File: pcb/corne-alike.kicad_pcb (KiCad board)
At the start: 2 copper layers, 45 parts, among them SW1 SW_PUSH, SW10 SW_PUSH, SW11 SW_PUSH, SW12 SW_PUSH, SW13 SW_PUSH, SW14 SW_PUSH, SW15 SW_PUSH, SW16 SW_PUSH, SW17 SW_PUSH, SW18 SW_PUSH, SW19 SW_PUSH, SW2 SW_PUSH, SW20 SW_PUSH, SW21 SW_PUSH, SW3 SW_PUSH, SW4 SW_PUSH, SW5 SW_PUSH, SW6 SW_PUSH, SW7 SW_PUSH, SW8 SW_PUSH, SW9 SW_PUSH, U1 nice_nano

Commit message: Place switches and create pcb shape
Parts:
- U1: value nice_nano -> ProMicro
- moved SW6 235.7 mm to (244.2, 40.8)
- moved SW5 210.3 mm to (226.0, 38.5)
- moved SW12 207.4 mm to (244.2, 58.0)
- moved SW4 185.8 mm to (207.8, 36.0)
- moved SW11 182.4 mm to (226.0, 55.8)
- moved SW18 179.2 mm to (244.2, 75.2)
- moved SW3 160.9 mm to (189.5, 38.5)
- moved SW21 159.0 mm to (259.3, 100.7), turned to 60 degrees
- moved SW10 158.4 mm to (207.8, 53.2)
- moved SW17 154.7 mm to (226.0, 73.0)
- moved SW20 142.2 mm to (238.8, 92.5)
- moved U1 140.9 mm to (264.8, 50.8)
- moved SW2 138.4 mm to (171.2, 50.0)
- moved SW9 134.9 mm to (189.5, 55.8)
- moved SW19 134.0 mm to (220.5, 92.5)
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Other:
- board outline added: 130.3 x 85.3 mm

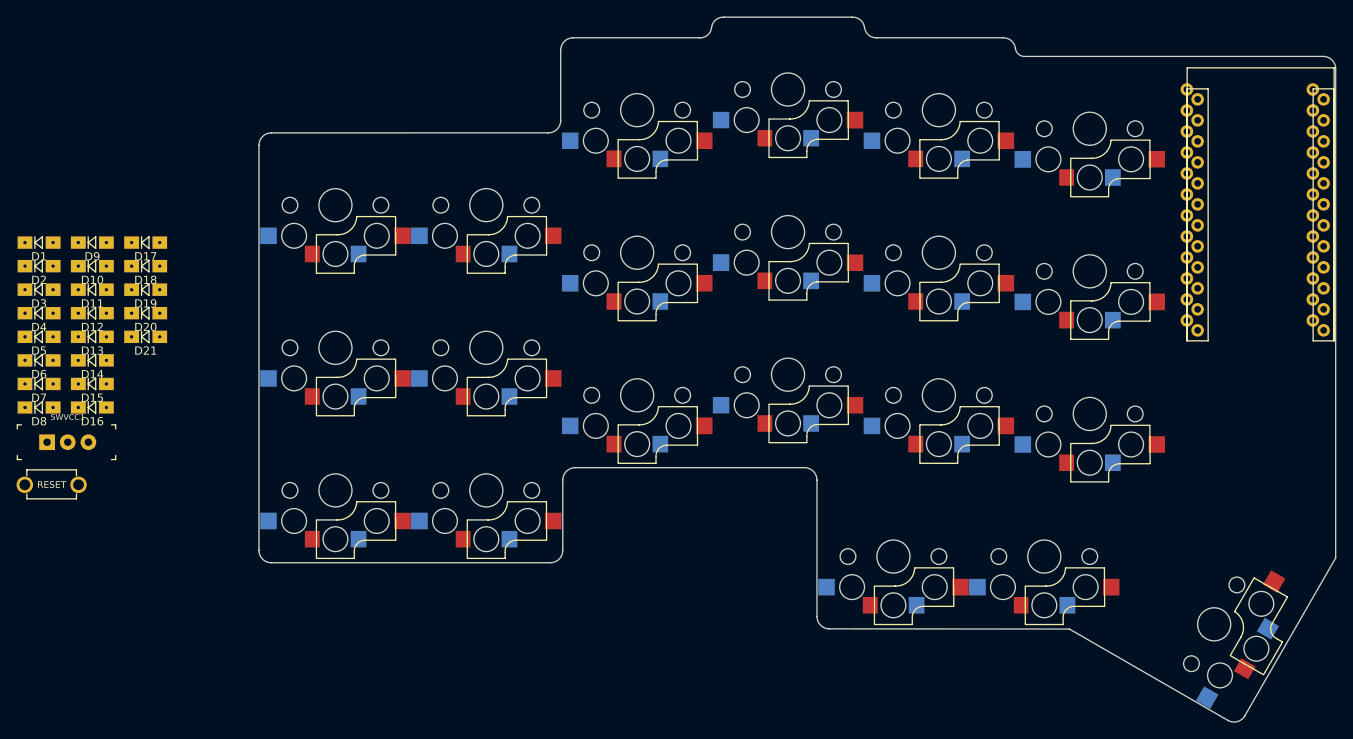
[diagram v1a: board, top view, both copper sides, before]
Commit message: Connect switches and diodes
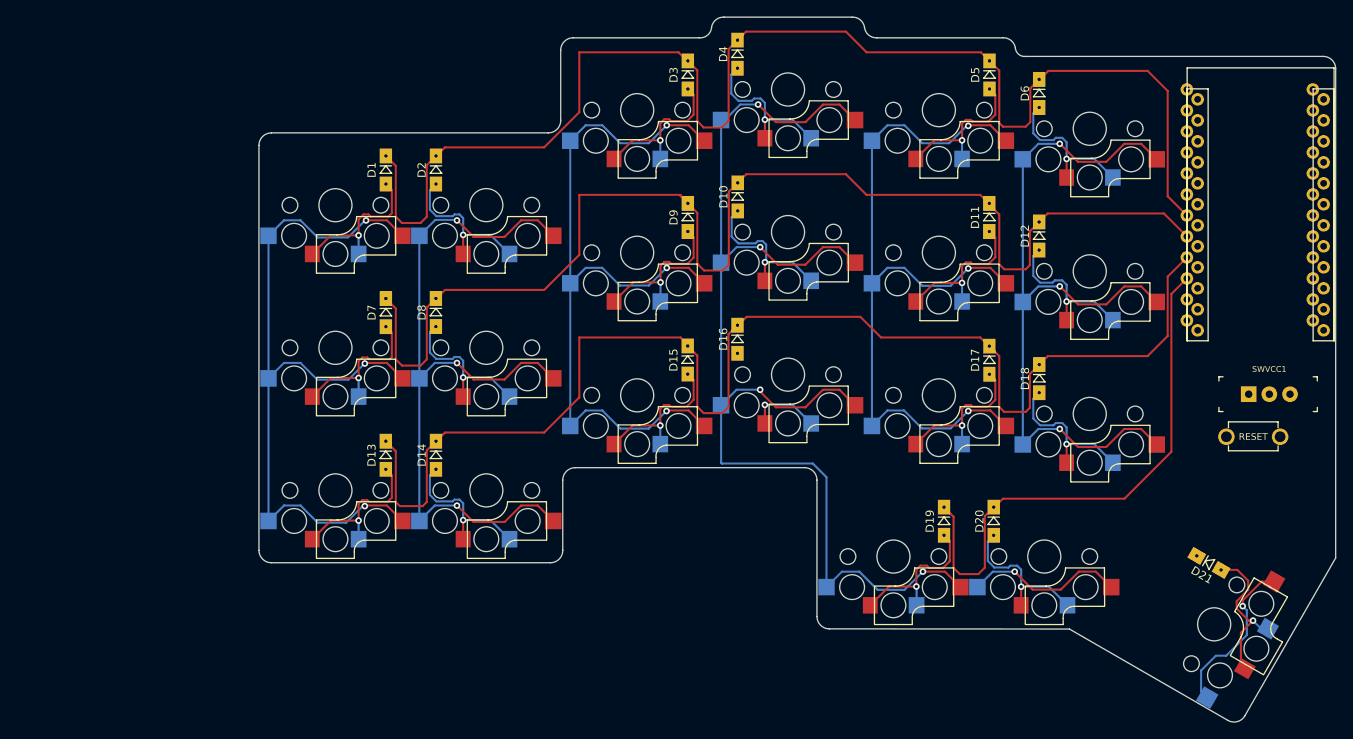
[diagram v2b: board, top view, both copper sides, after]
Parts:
- moved SWVCC1 145.5 mm to (263.5, 72.9)
- moved SWRST1 145.5 mm to (264.0, 78.0)
- moved D21 131.5 mm to (258.7, 93.3), turned to -30 degrees
- moved D6 125.2 mm to (238.1, 36.5), turned to -90 degrees
- moved D5 119.3 mm to (232.1, 34.2), turned to -90 degrees
- moved D12 114.9 mm to (238.1, 53.7), turned to -90 degrees
- moved D18 108.9 mm to (238.1, 71.0), turned to -90 degrees
- moved D11 108.9 mm to (232.1, 51.5), turned to -90 degrees
- moved D20 105.6 mm to (232.6, 88.2), turned to -90 degrees
- moved D17 103.1 mm to (232.1, 68.8), turned to -90 degrees
- moved D19 100.6 mm to (226.6, 88.2), turned to -90 degrees
- moved D4 90.1 mm to (201.6, 31.7), turned to -90 degrees
- moved D3 82.7 mm to (195.6, 34.2), turned to -90 degrees
- moved D10 78.5 mm to (201.7, 49.0), turned to -90 degrees
- moved D16 78.5 mm to (201.6, 66.2), turned to -90 degrees
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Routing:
- net row0: track 0.00 -> 166.3 mm
- net row2: track 0.00 -> 160.3 mm
- net row1: track 0.00 -> 152.6 mm
- net col3: track 0.00 -> 146.5 mm, vias 0 -> 4
- net col5: track 0.00 -> 113.2 mm, vias 0 -> 4
- net col4: track 0.00 -> 112.7 mm, vias 0 -> 4
- net col2: track 0.00 -> 93.4 mm, vias 0 -> 3
- net col0: track 0.00 -> 93.3 mm, vias 0 -> 3
- net col1: track 0.00 -> 92.9 mm, vias 0 -> 3
- net row3: track 0.00 -> 66.0 mm
- net Net-(D10-A): track 0.00 -> 19.2 mm, vias 0 -> 1
- net Net-(D7-A): track 0.00 -> 19.2 mm, vias 0 -> 1
- net Net-(D21-A): track 0.00 -> 19.2 mm, vias 0 -> 1
- net Net-(D1-A): track 0.00 -> 19.1 mm, vias 0 -> 1
- net Net-(D2-A): track 0.00 -> 19.1 mm, vias 0 -> 1
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
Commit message: Connect rows and cols
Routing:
- net col0: track 93.3 -> 240.3 mm, vias 3 -> 13
- net col1: track 92.9 -> 215.7 mm, vias 3 -> 11
- net col2: track 93.4 -> 188.3 mm, vias 3 -> 9
- net col4: track 112.7 -> 202.3 mm, vias 4 -> 6
- net col5: track 113.2 -> 197.1 mm
- net col3: track 146.5 -> 229.7 mm, vias 4 -> 8
- net GND: track 0.00 -> 48.5 mm
- net row3: track 66.0 -> 108.6 mm
- net row2: track 160.3 -> 177.6 mm
- net row0: track 166.3 -> 183.4 mm
- net row1: track 152.6 -> 169.6 mm
- net vcc: track 0.00 -> 14.4 mm
- net reset: track 0.00 -> 14.4 mm
- net Net-(D16-A): track 8.78 -> 19.2 mm

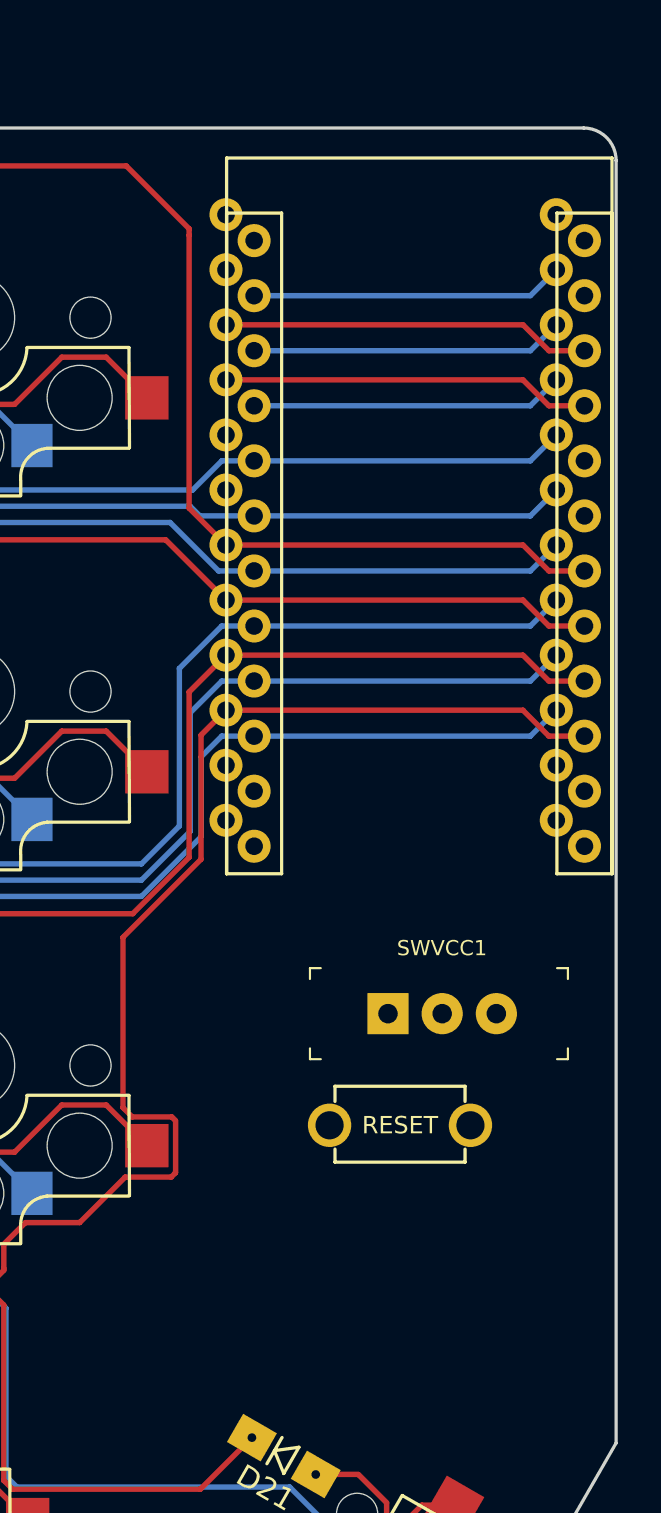
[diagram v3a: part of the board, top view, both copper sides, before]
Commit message: Add bat connector, place reset, on/off and bat to pcb
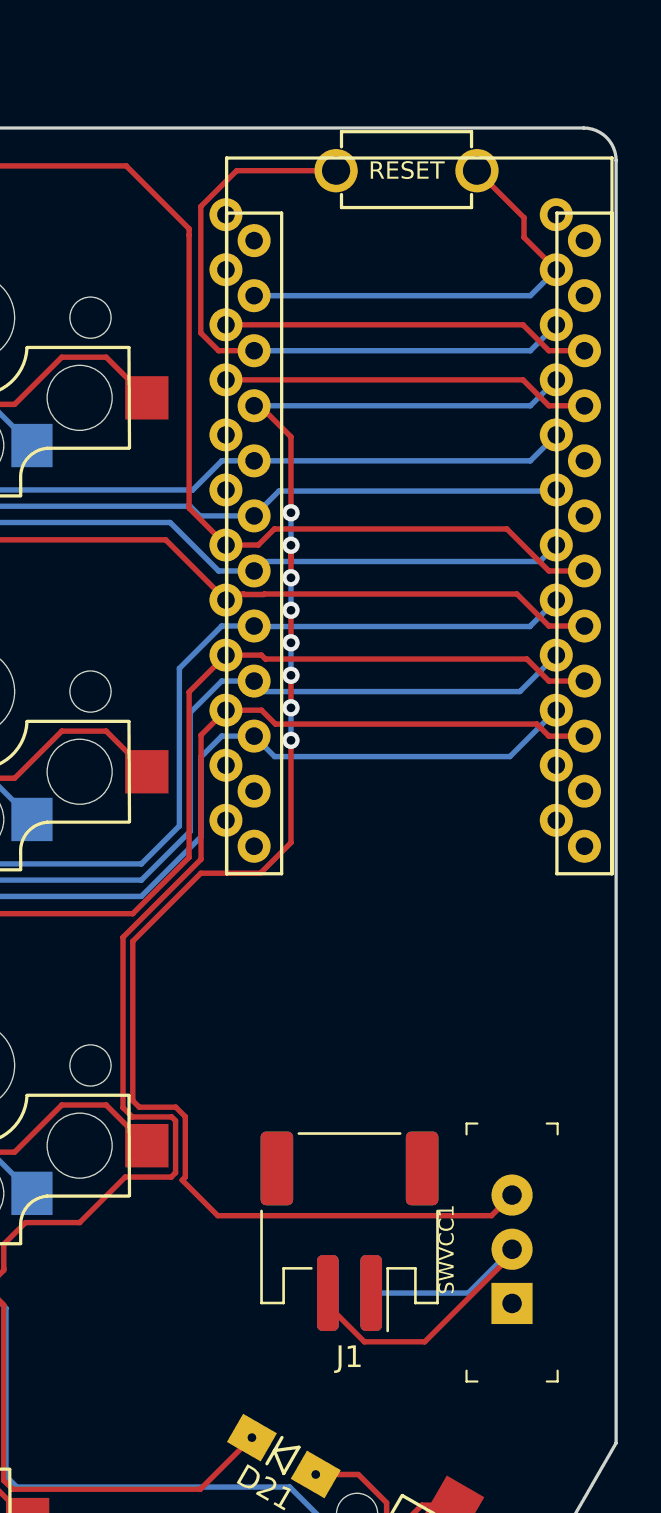
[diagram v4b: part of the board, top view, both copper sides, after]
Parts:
- added J1: Conn_01x02_Socket, corne-alike:JST_PH_S2B-PH-SM4-TB_1x02-1MP_P2.00mm_Horizontal, F.Cu at (261.7, 82.9)
- added J1: Conn_01x02_Socket, corne-alike:JST_PH_S2B-PH-SM4-TB_1x02-1MP_P2.00mm_Horizontal, B.Cu at (261.7, 82.9)
- U1: value ProMicro -> nice_nano
- moved SWRST1 44.0 mm to (264.3, 34.0)
- moved SWVCC1 14.5 mm to (269.2, 86.2), turned to 90 degrees
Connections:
- SWVCC1 pad 2: VCC -> Net-(J1-Pin_2)
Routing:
- net vcc: track 14.4 -> 75.6 mm, vias 0 -> 8
- net Net-(J1-Pin_2): track 0.00 -> 18.8 mm
- net reset: track 14.4 -> 30.1 mm
- net GND: track 48.5 -> 54.6 mm
- net col5: track 197.1 -> 197.9 mm
- net row0: track 183.4 -> 184.0 mm

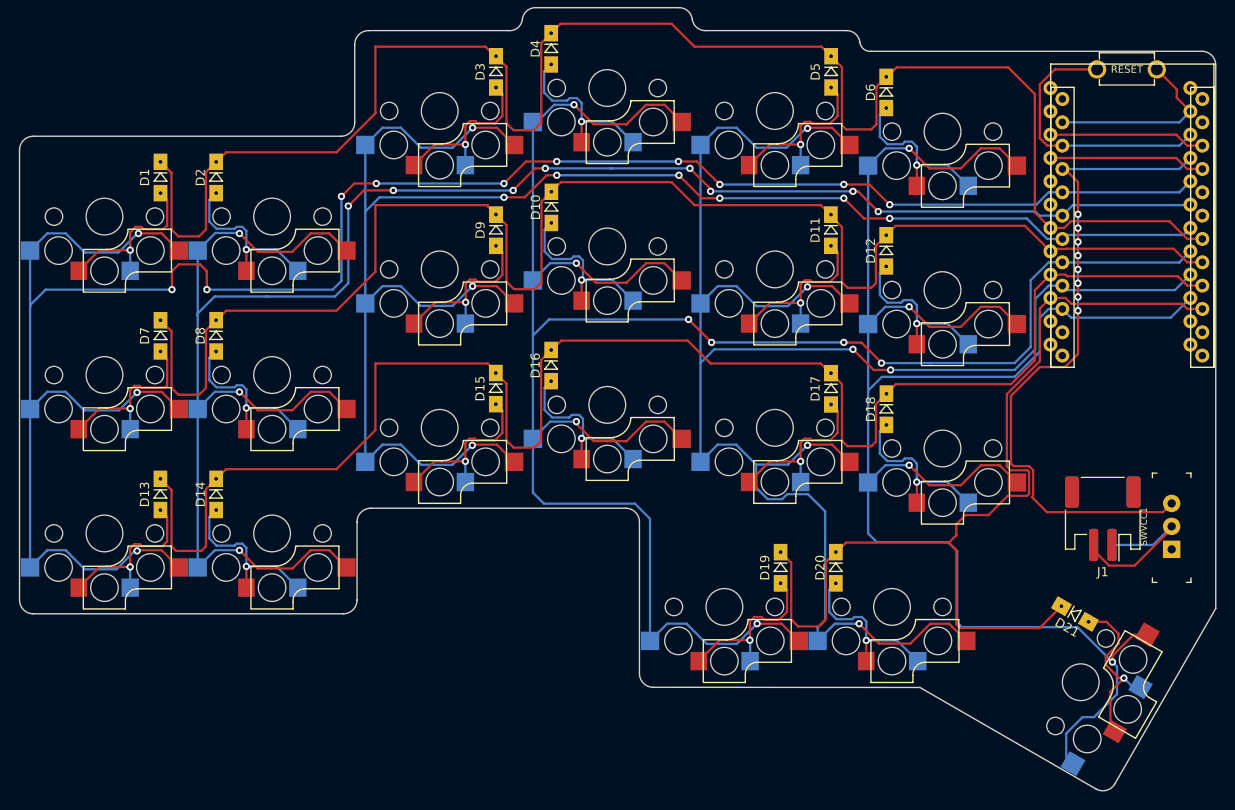
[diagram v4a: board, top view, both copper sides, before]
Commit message: Clean up tracks, drc violations
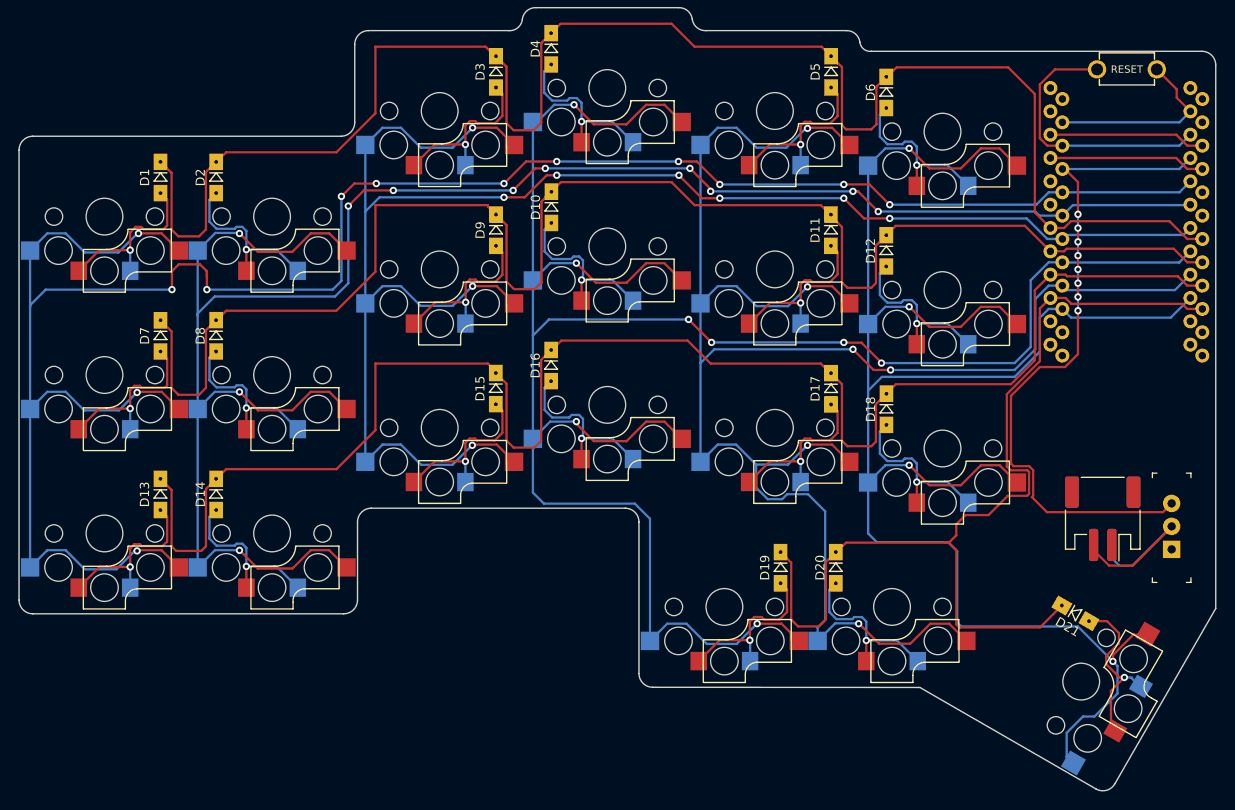
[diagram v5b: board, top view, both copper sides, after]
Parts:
- U1: value nice_nano -> ProMicro
- moved SW21 0.09 mm to (259.4, 100.6)
- moved D21 0.09 mm to (258.7, 93.2)
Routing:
- net Net-(#FLG01-pwr): track 18.8 -> 21.3 mm
- net vcc: track 75.6 -> 74.1 mm
- net col4: track 202.7 -> 201.6 mm
- net col0: track 240.3 -> 239.6 mm
- net Net-(D21-A): track 19.2 -> 18.5 mm
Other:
- outline, holes or cut-outs redrawn

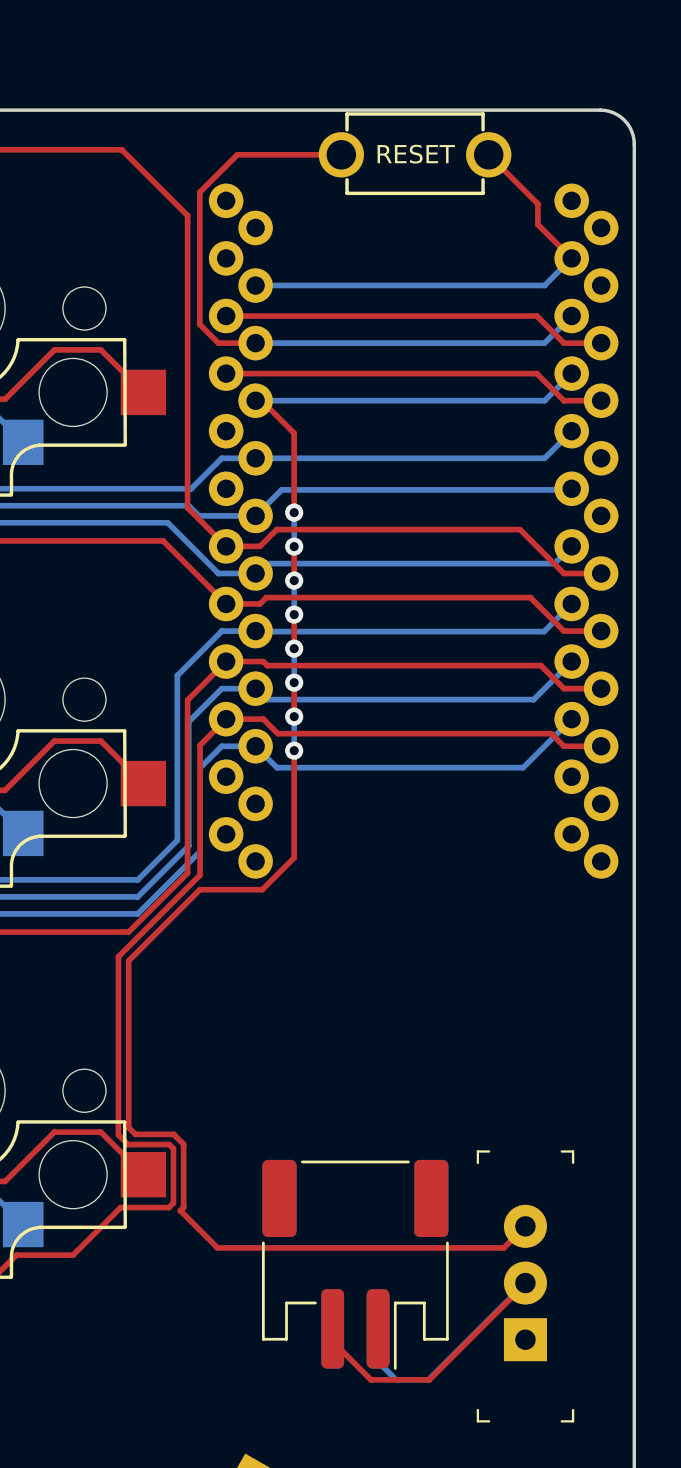
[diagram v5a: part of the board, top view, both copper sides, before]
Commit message: Trace GND, clean up controller escape
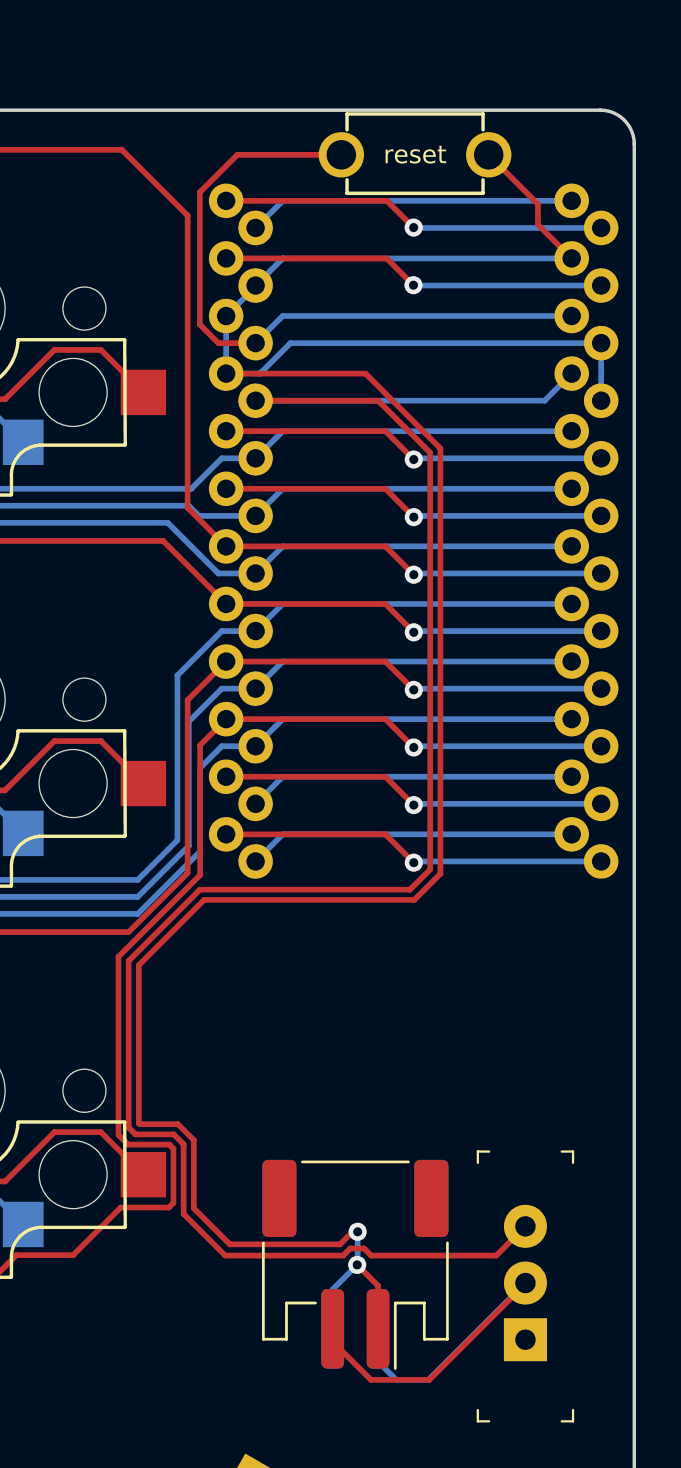
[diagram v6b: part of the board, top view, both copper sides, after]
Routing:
- net GND: track 54.6 -> 117.9 mm, vias 0 -> 2
- net unconnected-(U1-P1.06-Pad12): track 0.00 -> 17.1 mm, vias 0 -> 1
- net unconnected-(U1-P1.04-Pad11): track 0.00 -> 17.1 mm, vias 0 -> 1
- net unconnected-(U1-P0.20-Pad6): track 0.00 -> 17.1 mm, vias 0 -> 1
- net unconnected-(U1-P0.17-Pad5): track 0.00 -> 17.1 mm, vias 0 -> 1
- net unconnected-(U1-RX1/P0.08-Pad2): track 0.00 -> 17.0 mm, vias 0 -> 1
- net unconnected-(U1-TX0/P0.06-Pad1): track 0.00 -> 17.0 mm, vias 0 -> 1
- net unconnected-(U1-RAW/P0.04-Pad24): track 0.00 -> 14.4 mm
- net unconnected-(U1-NFC2/P0.10-Pad14): track 0.00 -> 14.4 mm
- net unconnected-(U1-NFC1/P0.09-Pad13): track 0.00 -> 14.4 mm
- net vcc: track 74.1 -> 86.2 mm, vias 8 -> 0
- net col5: track 197.9 -> 197.1 mm
- net row0: track 183.7 -> 183.1 mm, vias 0 -> 1
- net row1: track 169.8 -> 169.6 mm, vias 0 -> 1
- net row3: track 108.6 -> 108.7 mm, vias 0 -> 1
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
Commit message: Clean up tracks
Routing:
- net Net-(#FLG01-pwr): track 21.3 -> 19.3 mm
- net col5: track 197.1 -> 198.6 mm
- net row3: track 108.7 -> 108.1 mm
